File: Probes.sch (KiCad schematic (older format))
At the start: 16 parts, among them U3 INA333

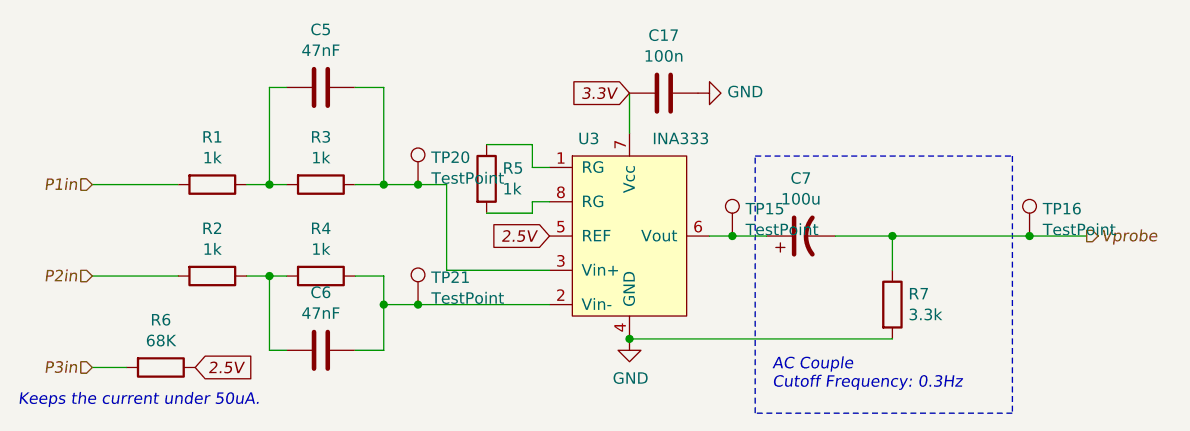
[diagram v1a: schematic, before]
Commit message: #24 - Updated AC couple
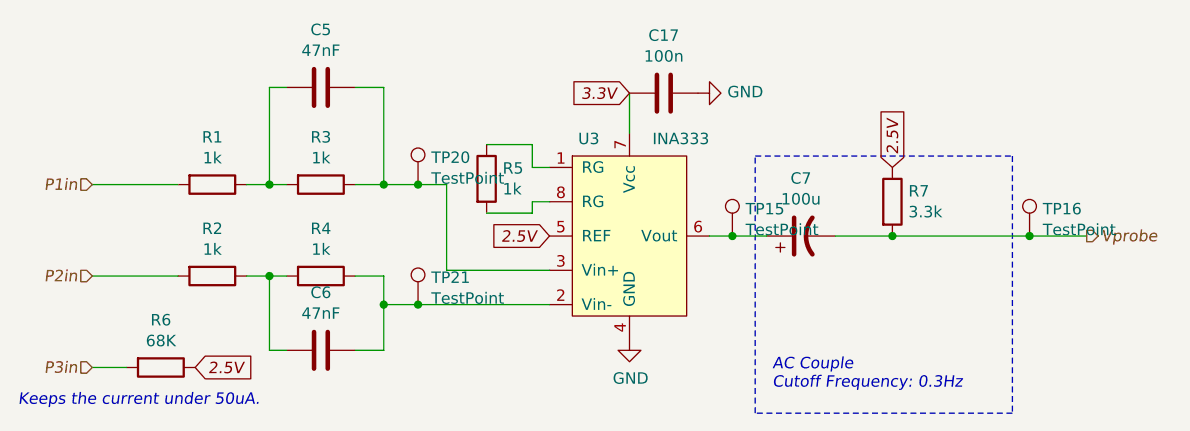
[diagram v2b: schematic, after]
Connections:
- net 2.5V: now also R7.1
- net GND: no longer R7.2
- net Vprobe: now also R7.2; no longer R7.1
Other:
- moved on the sheet: R7
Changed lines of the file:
@@
 L Device:R R7
 U 1 1 5FA0C9DE
-P 7250 3850
-F 0 "R7" H 7320 3896 50  0000 L CNN
-F 1 "3.3k" H 7320 3805 50  0000 L CNN
-F 2 "Resistor_SMD:R_0805_2012Metric_Pad1.20x1.40mm_HandSolder" V 7180 3850 50  0001 C CNN
-F 3 "~" H 7250 3850 50  0001 C CNN
-	1    7250 3850
+P 7250 3400
+F 0 "R7" H 7320 3446 50  0000 L CNN
+F 1 "3.3k" H 7320 3355 50  0000 L CNN
+F 2 "Resistor_SMD:R_0805_2012Metric_Pad1.20x1.40mm_HandSolder" V 7180 3400 50  0001 C CNN
+F 3 "~" H 7250 3400 50  0001 C CNN
+	1    7250 3400
 	1    0    0    -1
 $EndComp
@@
 Wire Wire Line
 	7000 3550 7250 3550
-Wire Wire Line
-	7250 3550 7250 3700
-Wire Wire Line
-	7250 4000 6100 4000
 Text Notes 6725 4225 0    50   Italic 0
 AC Couple\nCutoff Frequency: 0.3Hz
@@
 Wire Wire Line
 	6100 2925 6100 3100
-Connection ~ 6100 4000
 Wire Wire Line
 	3750 4125 3900 4125
@@
 Wire Wire Line
 	3750 3725 4125 3725
+Text GLabel 7250 3250 1    50   Input Italic 0
+2.5V
 $EndSCHEMATC
